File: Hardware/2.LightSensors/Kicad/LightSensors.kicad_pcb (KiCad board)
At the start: 2 copper layers, 45 x 25 mm, 21 parts, among them J1 Conn_01x10_Pin, U1 AS7331, U2 OPT3004

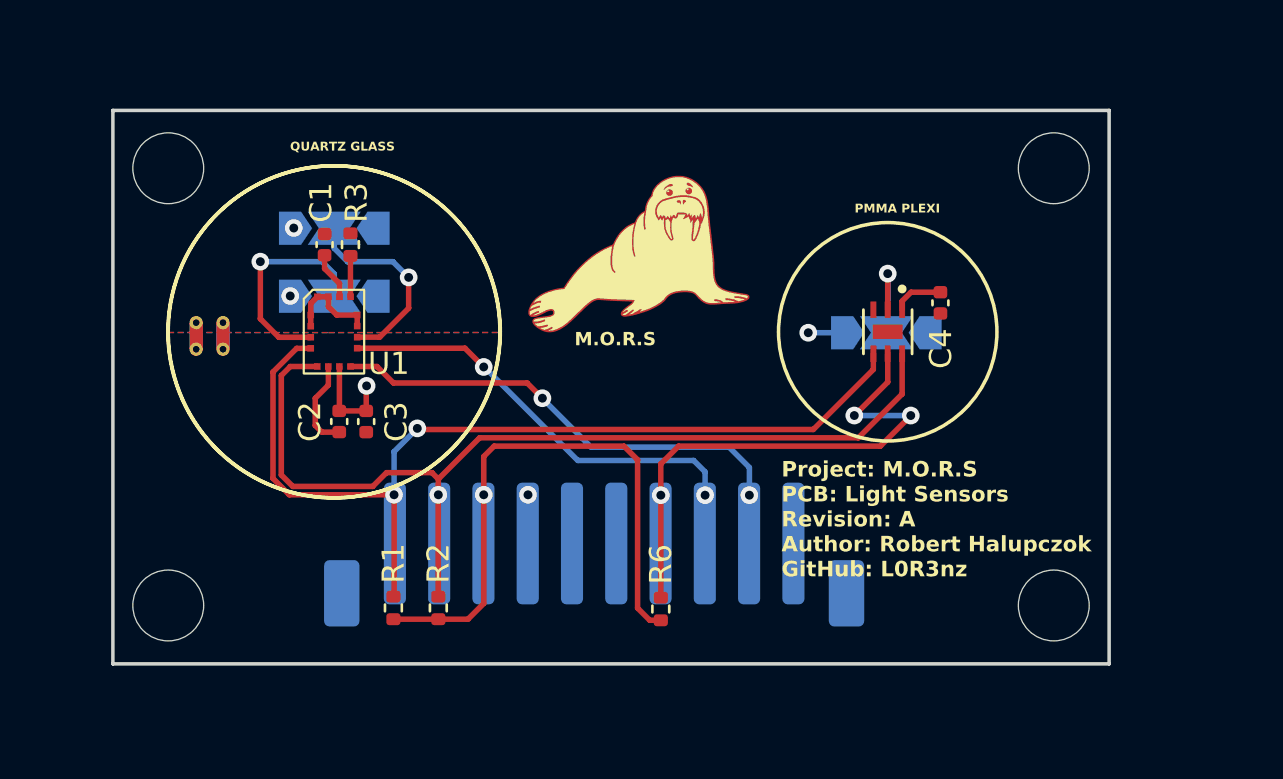
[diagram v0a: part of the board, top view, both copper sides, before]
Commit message: Update layout with changes made in schematic
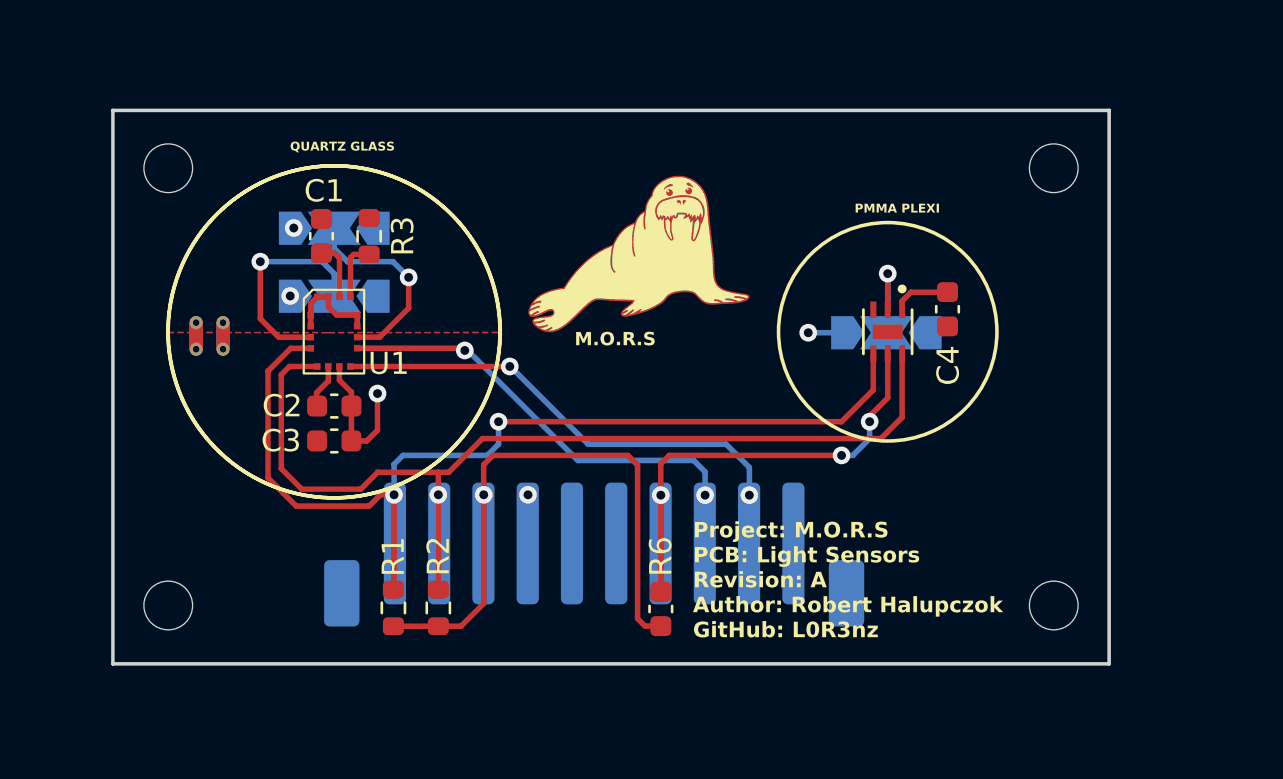
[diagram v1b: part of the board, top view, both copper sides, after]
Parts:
- C1, C2, C3, C4: footprint Capacitor_SMD:C_0402_1005Metric -> Capacitor_SMD:C_0603_1608Metric
- H1, H2, H3, H4: footprint MountingHole:MountingHole_3.2mm_M3 -> MountingHole:MountingHole_2.2mm_M2
- R1, R2, R3: footprint Resistor_SMD:R_0402_1005Metric -> Resistor_SMD:R_0603_1608Metric
- R6: footprint Resistor_SMD:R_0402_1005Metric -> Capacitor_SMD:C_0603_1608Metric
- moved C3 1.69 mm to (89.4, 120.2), turned to 180 degrees
- moved R3 0.93 mm to (90.9, 111.0)
- moved C2 0.73 mm to (89.4, 118.7), turned to 180 degrees
- moved C4 0.43 mm to (117.1, 114.3)
- moved C1 0.41 mm to (88.8, 111.0)
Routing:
- net OPT3004_INT: track 26.4 -> 22.4 mm
- net +3.3V: track 35.2 -> 37.7 mm
- net GND: track 5.65 -> 3.51 mm
- net I2C_SCL: track 43.2 -> 44.9 mm
- net Net-(U1-REXT): track 1.85 -> 2.63 mm
- net I2C_SDA: track 43.6 -> 44.3 mm
- net +3.3VA: track 2.15 -> 2.67 mm

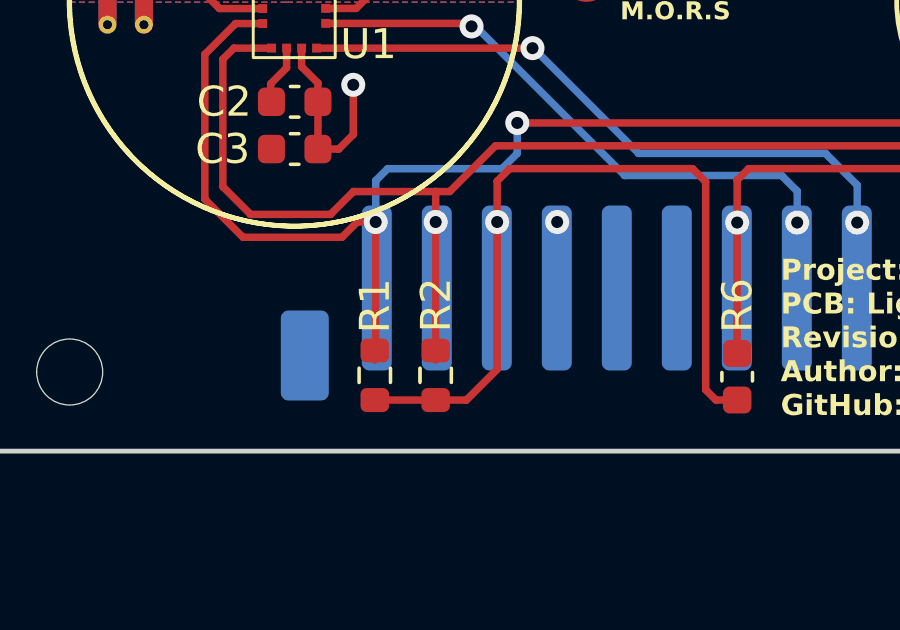
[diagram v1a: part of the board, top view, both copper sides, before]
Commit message: Add capacitor bettwen VCC and GND on PCB
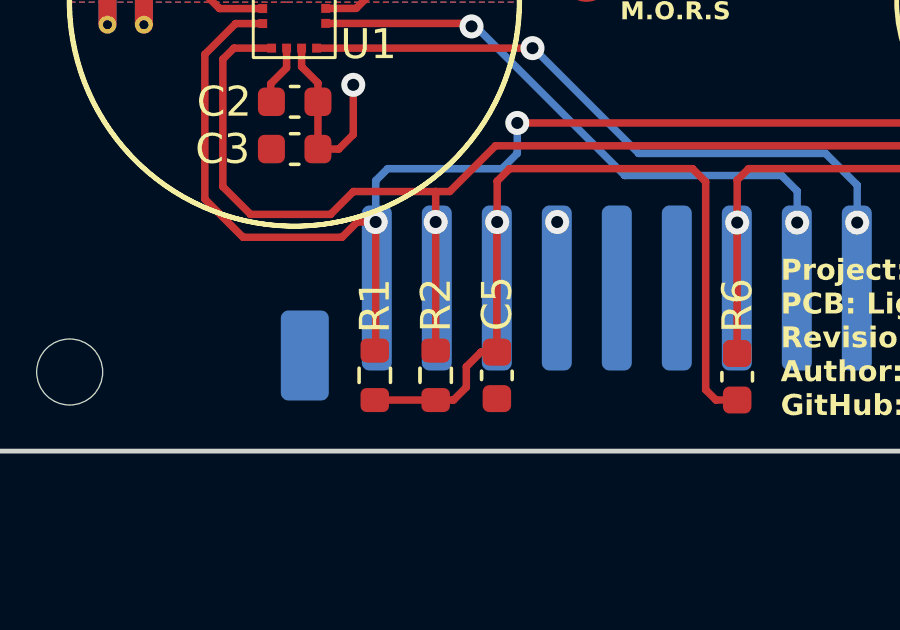
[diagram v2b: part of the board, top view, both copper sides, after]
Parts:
- added C5: 100nF, Capacitor_SMD:C_0603_1608Metric, F.Cu at (96.1, 127.8)
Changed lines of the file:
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@@
     (pad_to_mask_clearance 0)
     (aux_axis_origin 79.354 130.319335)
-    (grid_origin 101.854 0)
     (pcbplotparams
       (layerselection 0x00010fc_ffffffff)
@@
   (net 15 "Net-(U1-REXT)")
   (net 16 "unconnected-(J1-Pin_6-Pad6)")
+  (footprint "Capacitor_SMD:C_0603_1608Metric" (layer "F.Cu")
+    (at 96.094015 127.794026 -90)
+    (descr "Capacitor SMD 0603 (1608 Metric), square (rectangular) end terminal, IPC_7351 nominal, (Body size source: IPC-SM-782 page 76, https://www.pcb-3d.com/wordpress/wp-content/uploads/ipc-sm-782a_amendment_1_and_2.pdf), generated with kicad-footprint-generator")
+    (tags "capacitor")
+    (property "Sheetfile" "LightSensors.kicad_sch")
+    (property "Sheetname" "")
+    (property "ki_description" "Unpolarized capacitor")
+    (property "ki_keywords" "cap capacitor")
+    (attr smd)
+    (fp_text reference "C5" (at -2.391407 -0.005123 90) (layer "F.SilkS")
+        (effects (font (size 1 1) (thickness 0.15)))
+    )
+    (fp_text value "100nF" (at 0 1.43 90) (layer "F.Fab")
+        (effects (font (size 1 1) (thickness 0.15)))
+    )
+    (fp_text user "${REFERENCE}" (at 0 0 90) (layer "F.Fab")
+        (effects (font (size 0.4 0.4) (thickness 0.06)))
+    )
+    (fp_line (start -0.14058 -0.51) (end 0.14058 -0.51)
+      (stroke (width 0.12) (type solid)) (layer "F.SilkS"))
+    (fp_line (start -0.14058 0.51) (end 0.14058 0.51)
+      (stroke (width 0.12) (type solid)) (layer "F.SilkS"))
+    (fp_line (start -1.48 -0.73) (end 1.48 -0.73)
+      (stroke (width 0.05) (type solid)) (layer "F.CrtYd"))
+    (fp_line (start -1.48 0.73) (end -1.48 -0.73)
+      (stroke (width 0.05) (type solid)) (layer "F.CrtYd"))
+    (fp_line (start 1.48 -0.73) (end 1.48 0.73)
+      (stroke (width 0.05) (type solid)) (layer "F.CrtYd"))
+    (fp_line (start 1.48 0.73) (end -1.48 0.73)
+      (stroke (width 0.05) (type solid)) (layer "F.CrtYd"))
+    (fp_line (start -0.8 -0.4) (end 0.8 -0.4)
+      (stroke (width 0.1) (type solid)) (layer "F.Fab"))
+    (fp_line (start -0.8 0.4) (end -0.8 -0.4)
+      (stroke (width 0.1) (type solid)) (layer "F.Fab"))
+    (fp_line (start 0.8 -0.4) (end 0.8 0.4)
+      (stroke (width 0.1) (type solid)) (layer "F.Fab"))
+    (fp_line (start 0.8 0.4) (end -0.8 0.4)
+      (stroke (width 0.1) (type solid)) (layer "F.Fab"))
+    (pad "1" smd roundrect (at -0.775 0 270) (size 0.9 0.95) (layers "F.Cu" "F.Paste" "F.Mask") (roundrect_rratio 0.25)
+      (net 3 "+3.3V") (pintype "passive"))
+    (pad "2" smd roundrect (at 0.775 0 270) (size 0.9 0.95) (layers "F.Cu" "F.Paste" "F.Mask") (roundrect_rratio 0.25)
+      (net 4 "GND") (pintype "passive"))
+    (model "${KICAD6_3DMODEL_DIR}/Capacitor_SMD.3dshapes/C_0603_1608Metric.wrl"
+      (offset (xyz 0 0 0))
+      (scale (xyz 1 1 1))
+      (rotate (xyz 0 0 0))
+    )
+  )
   (footprint "MountingHole:MountingHole_2.2mm_M2" (layer "F.Cu")
     (at 121.854 127.682)
@@
   (via (at 87.524 110.632) (size 0.8) (drill 0.4) (layers "F.Cu" "B.Cu") (net 2))
   (via (at 87.364 113.702) (size 0.8) (drill 0.4) (layers "F.Cu" "B.Cu") (net 2))
+  (segment (start 96.094015 127.019026) (end 95.564469 127.019026) (width 0.25) (layer "F.Cu") (net 3))
   (segment (start 103.054 121.342) (end 102.616 120.904) (width 0.25) (layer "F.Cu") (net 3))
   (segment (start 90.129 118.05) (end 90.129 118.675) (width 0.25) (layer "F.Cu") (net 3))
   (segment (start 115.004 114.324335) (end 115.004 113.932) (width 0.25) (layer "F.Cu") (net 3))
+  (segment (start 95.075495 127.508) (end 95.075495 128.190505) (width 0.25) (layer "F.Cu") (net 3))
   (segment (start 103.394 128.615) (end 103.054 128.275) (width 0.25) (layer "F.Cu") (net 3))
+  (segment (start 96.094015 127.019026) (end 96.094015 122.691985) (width 0.25) (layer "F.Cu") (net 3))
   (segment (start 103.054 128.275) (end 103.054 121.342) (width 0.25) (layer "F.Cu") (net 3))
-  (segment (start 94.054 128.617) (end 95.079 128.617) (width 0.25) (layer "F.Cu") (net 3))
+  (segment (start 94.649 128.617) (end 94.054 128.617) (width 0.25) (layer "F.Cu") (net 3))
   (segment (start 91.307182 119.766818) (end 90.824 120.25) (width 0.25) (layer "F.Cu") (net 3))
-  (segment (start 95.079 128.617) (end 96.104 127.592) (width 0.25) (layer "F.Cu") (net 3))
   (segment (start 91.307182 118.11) (end 91.307182 119.766818) (width 0.25) (layer "F.Cu") (net 3))
   (segment (start 90.129 120.25) (end 90.129 118.675) (width 0.25) (layer "F.Cu") (net 3))
   (segment (start 117.047 113.532) (end 117.054 113.525) (width 0.25) (layer "F.Cu") (net 3))
+  (segment (start 95.564469 127.019026) (end 95.075495 127.508) (width 0.25) (layer "F.Cu") (net 3))
   (segment (start 89.584341 117.505341) (end 90.129 118.05) (width 0.25) (layer "F.Cu") (net 3))
   (segment (start 115.404 113.532) (end 117.047 113.532) (width 0.25) (layer "F.Cu") (net 3))
@@
   (segment (start 96.52 120.904) (end 96.104 121.32) (width 0.25) (layer "F.Cu") (net 3))
   (segment (start 90.824 120.25) (end 90.129 120.25) (width 0.25) (layer "F.Cu") (net 3))
-  (segment (start 96.104 127.592) (end 96.104 122.682) (width 0.25) (layer "F.Cu") (net 3))
+  (segment (start 95.075495 128.190505) (end 94.649 128.617) (width 0.25) (layer "F.Cu") (net 3))
   (segment (start 89.584341 116.886913) (end 89.584341 117.505341) (width 0.25) (layer "F.Cu") (net 3))
   (segment (start 92.024 128.617) (end 94.054 128.617) (width 0.25) (layer "F.Cu") (net 3))
@@
   (via (at 96.104 122.682) (size 0.8) (drill 0.4) (layers "F.Cu" "B.Cu") (net 3))
   (via (at 91.307182 118.11) (size 0.8) (drill 0.4) (layers "F.Cu" "B.Cu") (net 3))
-  (segment (start 96.092 122.67) (end 96.104 122.682) (width 0.25) (layer "B.Cu") (net 3))
   (segment (start 96.092 124.882) (end 96.092 122.694) (width 0.25) (layer "B.Cu") (net 3))
-  (segment (start 96.092 122.694) (end 96.104 122.682) (width 0.25) (layer "B.Cu") (net 3))
   (segment (start 89.084341 117.544659) (end 89.084341 116.886913) (width 0.25) (layer "F.Cu") (net 4))
   (segment (start 88.554 118.65) (end 88.554 118.075) (width 0.25) (layer "F.Cu") (net 4))
@@
   (via (at 110.764 115.362) (size 0.8) (drill 0.4) (layers "F.Cu" "B.Cu") (net 4))
   (segment (start 112.294 115.362) (end 110.764 115.362) (width 0.25) (layer "B.Cu") (net 4))
+  (segment (start 92.054 126.937) (end 92.054 122.682) (width 0.25) (layer "F.Cu") (net 5))
   (segment (start 91.44 122.682) (end 90.932 123.19) (width 0.25) (layer "F.Cu") (net 5))
   (segment (start 87.63 123.19) (end 86.36 121.92) (width 0.25) (layer "F.Cu") (net 5))
@@
   (segment (start 96.774 119.38) (end 112.268 119.38) (width 0.25) (layer "F.Cu") (net 5))
   (segment (start 112.268 119.38) (end 113.704 117.944) (width 0.25) (layer "F.Cu") (net 5))
-  (segment (start 92.054 127.252) (end 92.054 122.682) (width 0.25) (layer "F.Cu") (net 5))
   (segment (start 86.36 117.094) (end 87.387087 116.066913) (width 0.25) (layer "F.Cu") (net 5))
   (segment (start 87.387087 116.066913) (end 88.289341 116.066913) (width 0.25) (layer "F.Cu") (net 5))
   (segment (start 86.36 121.92) (end 86.36 117.094) (width 0.25) (layer "F.Cu") (net 5))
   (segment (start 92.054 122.682) (end 91.44 122.682) (width 0.25) (layer "F.Cu") (net 5))
-  (segment (start 92.024 127.282) (end 92.054 127.252) (width 0.25) (layer "F.Cu") (net 5))
   (via (at 92.054 122.682) (size 0.8) (drill 0.4) (layers "F.Cu" "B.Cu") (net 5))
   (via (at 96.774 119.38) (size 0.8) (drill 0.4) (layers "F.Cu" "B.Cu") (net 5))
@@
   (segment (start 114.046 120.142) (end 96.04891 120.142) (width 0.25) (layer "F.Cu") (net 6))
   (segment (start 115.004 119.184) (end 114.046 120.142) (width 0.25) (layer "F.Cu") (net 6))
-  (segment (start 94.054 127.282) (end 94.054 122.682) (width 0.25) (layer "F.Cu") (net 6))
   (segment (start 94.054 121.666) (end 91.313 121.666) (width 0.25) (layer "F.Cu") (net 6))
   (segment (start 87.329087 116.886913) (end 88.584341 116.886913) (width 0.25) (layer "F.Cu") (net 6))
@@
   (segment (start 90.551 122.428) (end 87.884 122.428) (width 0.25) (layer "F.Cu") (net 6))
   (segment (start 94.054 121.666) (end 94.054 122.682) (width 0.25) (layer "F.Cu") (net 6))
+  (segment (start 94.054 126.967) (end 94.054 122.682) (width 0.25) (layer "F.Cu") (net 6))
   (via (at 94.054 122.682) (size 0.8) (drill 0.4) (layers "F.Cu" "B.Cu") (net 6))
   (segment (start 112.268 120.904) (end 104.486 120.904) (width 0.25) (layer "F.Cu") (net 8))
